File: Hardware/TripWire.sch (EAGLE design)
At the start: 40 parts, among them X1 GADGETEER-SOCKET

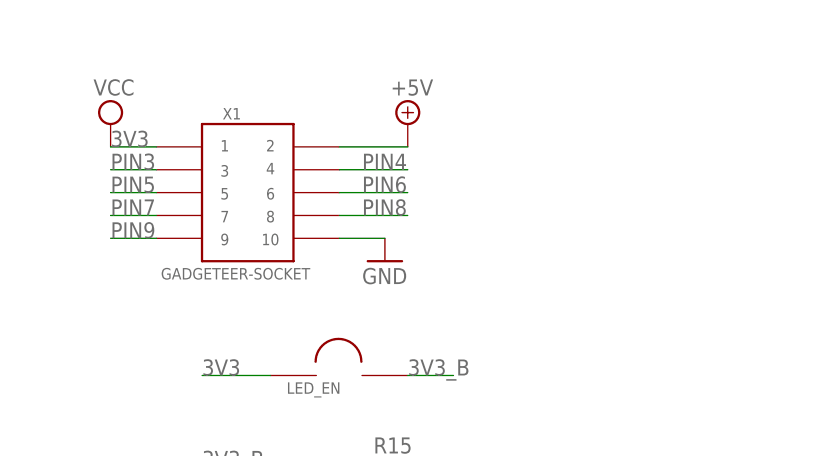
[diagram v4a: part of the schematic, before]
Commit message: Added pin breakout for non-Gadgeteer use.
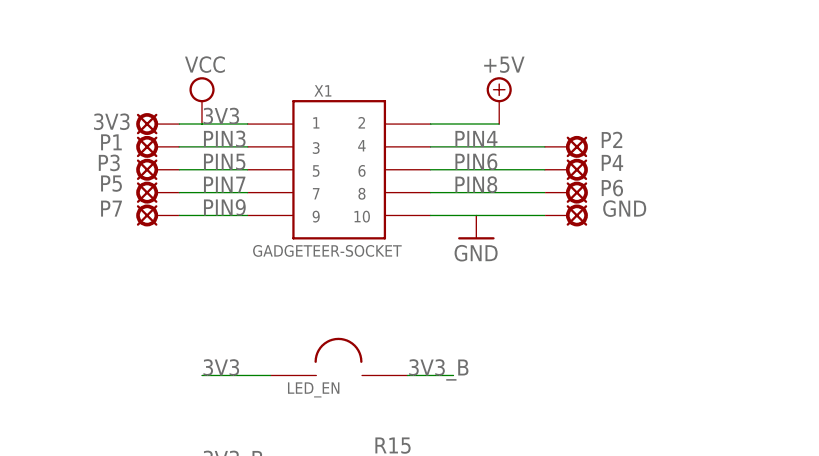
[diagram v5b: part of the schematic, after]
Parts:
- added 3V3, GND, P1, P2, P3, P4, P5, P6, P7: LSP11, solpad:LSP11
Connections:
- net 3V3: now also 3V3.MP
- net GND: now also GND.MP
- net PIN3: now also P1.MP
- net PIN4: now also P2.MP
- net PIN5: now also P3.MP
- net PIN6: now also P4.MP
- net PIN7: now also P5.MP
- net PIN8: now also P6.MP
- net PIN9: now also P7.MP
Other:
- moved on the sheet: X1
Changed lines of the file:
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@@
 <part name="R21" library="SparkFun-Resistors" deviceset="RESISTOR" device="0603-RES" value="33"/>
 <part name="LED_EN" library="SoftDust" deviceset="SOLDER-JUNCTION" device=""/>
+<part name="P2" library="solpad" deviceset="LSP11" device=""/>
+<part name="P4" library="solpad" deviceset="LSP11" device=""/>
+<part name="P6" library="solpad" deviceset="LSP11" device=""/>
+<part name="GND" library="solpad" deviceset="LSP11" device=""/>
+<part name="3V3" library="solpad" deviceset="LSP11" device=""/>
+<part name="P1" library="solpad" deviceset="LSP11" device=""/>
+<part name="P3" library="solpad" deviceset="LSP11" device=""/>
+<part name="P5" library="solpad" deviceset="LSP11" device=""/>
+<part name="P7" library="solpad" deviceset="LSP11" device=""/>
 </parts>
 <sheets>
@@
 <instances>
 <instance part="FRAME2" gate="G$1" x="0" y="0"/>
-<instance part="GND1" gate="1" x="45.72" y="101.6"/>
-<instance part="V1" gate="+5V" x="48.26" y="116.84"/>
-<instance part="V2" gate="G$1" x="15.24" y="116.84"/>
-<instance part="X1" gate="G$1" x="30.48" y="109.22" smashed="yes">
-<attribute name="NAME" x="27.686" y="117.348" size="1.27" layer="95"/>
-<attribute name="VALUE" x="20.828" y="99.568" size="1.27" layer="96"/>
+<instance part="GND1" gate="1" x="55.88" y="104.14"/>
+<instance part="V1" gate="+5V" x="58.42" y="119.38"/>
+<instance part="V2" gate="G$1" x="25.4" y="119.38"/>
+<instance part="X1" gate="G$1" x="40.64" y="111.76" smashed="yes">
+<attribute name="NAME" x="37.846" y="119.888" size="1.27" layer="95"/>
+<attribute name="VALUE" x="30.988" y="102.108" size="1.27" layer="96"/>
 </instance>
 <instance part="LOGO1" gate="G$1" x="10.16" y="7.62"/>
@@
 <attribute name="NAME" x="34.798" y="86.868" size="1.27" layer="95"/>
 </instance>
+<instance part="P2" gate="1" x="66.04" y="114.3" smashed="yes" rot="R270">
+<attribute name="NAME" x="69.596" y="114.173" size="1.778" layer="95"/>
+</instance>
+<instance part="P4" gate="1" x="66.04" y="111.76" smashed="yes" rot="R270">
+<attribute name="NAME" x="69.596" y="111.633" size="1.778" layer="95"/>
+</instance>
+<instance part="P6" gate="1" x="66.04" y="109.22" smashed="yes" rot="R270">
+<attribute name="NAME" x="69.596" y="108.839" size="1.778" layer="95"/>
+</instance>
+<instance part="GND" gate="1" x="66.04" y="106.68" smashed="yes" rot="R270">
+<attribute name="NAME" x="69.85" y="106.553" size="1.778" layer="95"/>
+</instance>
+<instance part="3V3" gate="1" x="20.32" y="116.84" smashed="yes" rot="R90">
+<attribute name="NAME" x="17.526" y="117.983" size="1.778" layer="95" rot="R180"/>
+</instance>
+<instance part="P1" gate="1" x="20.32" y="114.3" smashed="yes" rot="R90">
+<attribute name="NAME" x="13.97" y="113.919" size="1.778" layer="95"/>
+</instance>
+<instance part="P3" gate="1" x="20.32" y="111.76" smashed="yes" rot="R90">
+<attribute name="NAME" x="13.716" y="111.633" size="1.778" layer="95"/>
+</instance>
+<instance part="P5" gate="1" x="20.32" y="109.22" smashed="yes" rot="R90">
+<attribute name="NAME" x="13.97" y="109.347" size="1.778" layer="95"/>
+</instance>
+<instance part="P7" gate="1" x="20.32" y="106.68" smashed="yes" rot="R90">
+<attribute name="NAME" x="13.97" y="106.553" size="1.778" layer="95"/>
+</instance>
 </instances>
 <busses>
@@
 <net name="3V3" class="1">
 <segment>
-<wire x1="15.24" y1="114.3" x2="20.32" y2="114.3" width="0.1524" layer="91"/>
 <pinref part="V2" gate="G$1" pin="VCC"/>
 <pinref part="X1" gate="G$1" pin="P$1"/>
-<label x="15.24" y="114.3" size="1.778" layer="95"/>
+<label x="25.4" y="116.84" size="1.778" layer="95"/>
+<pinref part="3V3" gate="1" pin="MP"/>
+<wire x1="25.4" y1="116.84" x2="30.48" y2="116.84" width="0.1524" layer="91"/>
+<wire x1="22.86" y1="116.84" x2="25.4" y2="116.84" width="0.1524" layer="91"/>
 </segment>
 <segment>
@@
 <net name="GND" class="1">
 <segment>
-<wire x1="45.72" y1="104.14" x2="40.64" y2="104.14" width="0.1524" layer="91"/>
+<wire x1="55.88" y1="106.68" x2="50.8" y2="106.68" width="0.1524" layer="91"/>
 <pinref part="GND1" gate="1" pin="GND"/>
 <pinref part="X1" gate="G$1" pin="P$10"/>
+<pinref part="GND" gate="1" pin="MP"/>
+<wire x1="63.5" y1="106.68" x2="55.88" y2="106.68" width="0.1524" layer="91"/>
 </segment>
 <segment>
@@
 <net name="+5V" class="1">
 <segment>
-<wire x1="48.26" y1="114.3" x2="40.64" y2="114.3" width="0.1524" layer="91"/>
+<wire x1="58.42" y1="116.84" x2="50.8" y2="116.84" width="0.1524" layer="91"/>
 <pinref part="V1" gate="+5V" pin="+5V"/>
 <pinref part="X1" gate="G$1" pin="P$2"/>
@@
 <segment>
 <pinref part="X1" gate="G$1" pin="P$3"/>
-<wire x1="20.32" y1="111.76" x2="15.24" y2="111.76" width="0.1524" layer="91"/>
-<label x="15.24" y="111.76" size="1.778" layer="95"/>
+<wire x1="30.48" y1="114.3" x2="22.86" y2="114.3" width="0.1524" layer="91"/>
+<label x="25.4" y="114.3" size="1.778" layer="95"/>
+<pinref part="P1" gate="1" pin="MP"/>
 </segment>
 <segment>
@@
 <segment>
 <pinref part="X1" gate="G$1" pin="P$4"/>
-<wire x1="40.64" y1="111.76" x2="48.26" y2="111.76" width="0.1524" layer="91"/>
-<label x="43.18" y="111.76" size="1.778" layer="95"/>
+<wire x1="50.8" y1="114.3" x2="63.5" y2="114.3" width="0.1524" layer="91"/>
+<label x="53.34" y="114.3" size="1.778" layer="95"/>
+<pinref part="P2" gate="1" pin="MP"/>
 </segment>
 <segment>
@@
 <segment>
 <pinref part="X1" gate="G$1" pin="P$5"/>
-<wire x1="20.32" y1="109.22" x2="15.24" y2="109.22" width="0.1524" layer="91"/>
-<label x="15.24" y="109.22" size="1.778" layer="95"/>
+<label x="25.4" y="111.76" size="1.778" layer="95"/>
+<pinref part="P3" gate="1" pin="MP"/>
+<wire x1="22.86" y1="111.76" x2="30.48" y2="111.76" width="0.1524" layer="91"/>
 </segment>
 <segment>
@@
 <segment>
 <pinref part="X1" gate="G$1" pin="P$7"/>
-<wire x1="20.32" y1="106.68" x2="15.24" y2="106.68" width="0.1524" layer="91"/>
-<label x="15.24" y="106.68" size="1.778" layer="95"/>
+<label x="25.4" y="109.22" size="1.778" layer="95"/>
+<pinref part="P5" gate="1" pin="MP"/>
+<wire x1="22.86" y1="109.22" x2="30.48" y2="109.22" width="0.1524" layer="91"/>
 </segment>
 <segment>
@@
 <segment>
 <pinref part="X1" gate="G$1" pin="P$9"/>
-<wire x1="20.32" y1="104.14" x2="15.24" y2="104.14" width="0.1524" layer="91"/>
-<label x="15.24" y="104.14" size="1.778" layer="95"/>
+<label x="25.4" y="106.68" size="1.778" layer="95"/>
+<pinref part="P7" gate="1" pin="MP"/>
+<wire x1="22.86" y1="106.68" x2="30.48" y2="106.68" width="0.1524" layer="91"/>
 </segment>
 <segment>
@@
 <segment>
 <pinref part="X1" gate="G$1" pin="P$6"/>
-<wire x1="40.64" y1="109.22" x2="48.26" y2="109.22" width="0.1524" layer="91"/>
-<label x="43.18" y="109.22" size="1.778" layer="95"/>
+<wire x1="50.8" y1="111.76" x2="63.5" y2="111.76" width="0.1524" layer="91"/>
+<label x="53.34" y="111.76" size="1.778" layer="95"/>
+<pinref part="P4" gate="1" pin="MP"/>
 </segment>
 <segment>
@@
 <segment>
 <pinref part="X1" gate="G$1" pin="P$8"/>
-<wire x1="40.64" y1="106.68" x2="48.26" y2="106.68" width="0.1524" layer="91"/>
-<label x="43.18" y="106.68" size="1.778" layer="95"/>
-</segment>
-<segment>
+<wire x1="50.8" y1="109.22" x2="63.5" y2="109.22" width="0.1524" layer="91"/>
+<label x="53.34" y="109.22" size="1.778" layer="95"/>
+<pinref part="P6" gate="1" pin="MP"/>
+</segment>
+<segment>

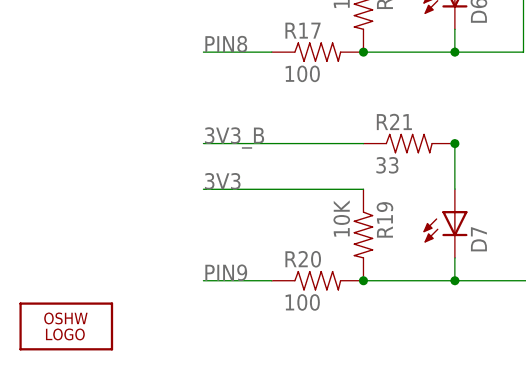
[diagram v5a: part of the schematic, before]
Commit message: Updated OSHW logo.
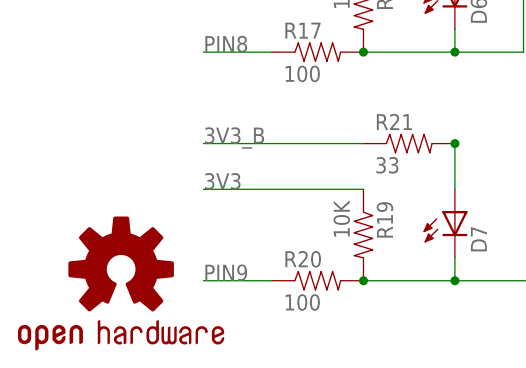
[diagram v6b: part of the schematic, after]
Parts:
- LOGO1: value LOGO-OSHW-FILLX0200-NT -> OSHW-LOGOM; device Logo:LOGO-OSHW-FILLX0200-NT -> SparkFun-Aesthetics:OSHW-LOGOM
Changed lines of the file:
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@@
 <part name="V2" library="supply2" deviceset="VCC" device=""/>
 <part name="X1" library="SoftDust" deviceset="GADGETEER-SOCKET" device=""/>
-<part name="LOGO1" library="Logo" deviceset="LOGO-OSHW-FILL" device="X0200-NT"/>
+<part name="LOGO1" library="SparkFun-Aesthetics" deviceset="OSHW-LOGO" device="M"/>
 <part name="U$1" library="SoftDust" deviceset="SPADE-TERMINAL" device="PTH"/>
 <part name="U$2" library="SoftDust" deviceset="SPADE-TERMINAL" device="PTH"/>
@@
 <attribute name="VALUE" x="30.988" y="102.108" size="1.27" layer="96"/>
 </instance>
-<instance part="LOGO1" gate="G$1" x="10.16" y="7.62"/>
+<instance part="LOGO1" gate="G$1" x="16.256" y="13.97"/>
 <instance part="U$1" gate="G$1" x="119.38" y="109.22"/>
 <instance part="U$2" gate="G$1" x="119.38" y="106.68"/>

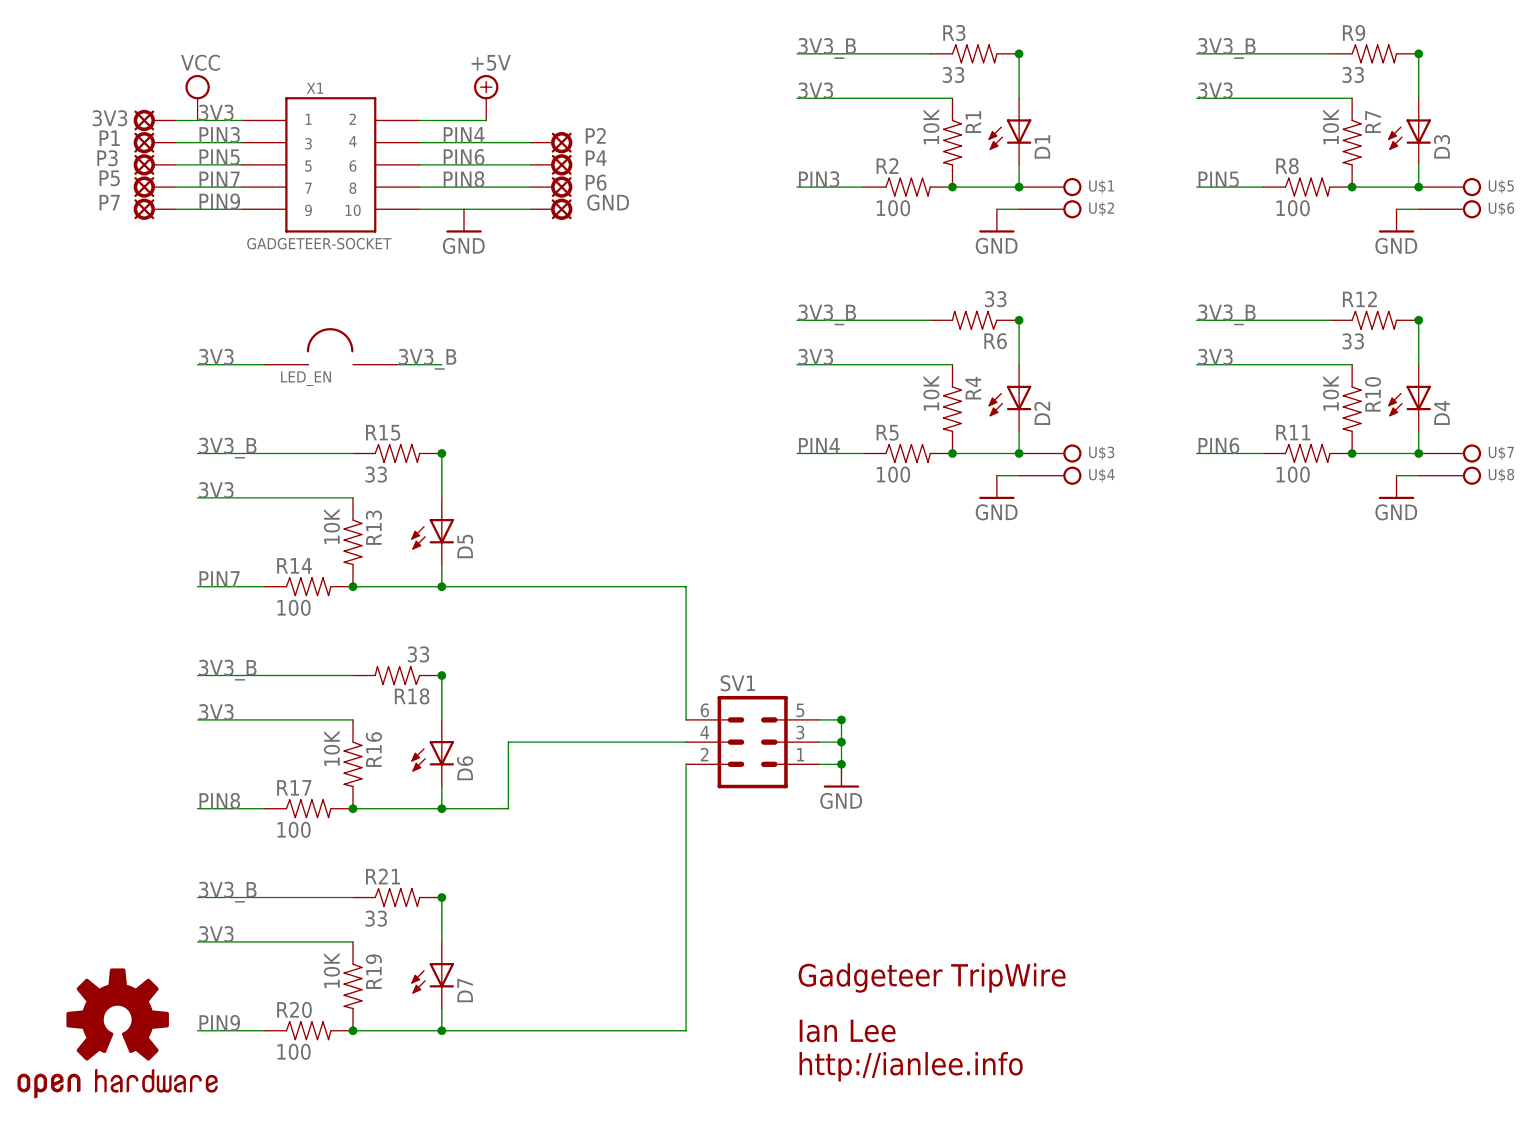
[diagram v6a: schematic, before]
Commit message: Added pin protection diodes.
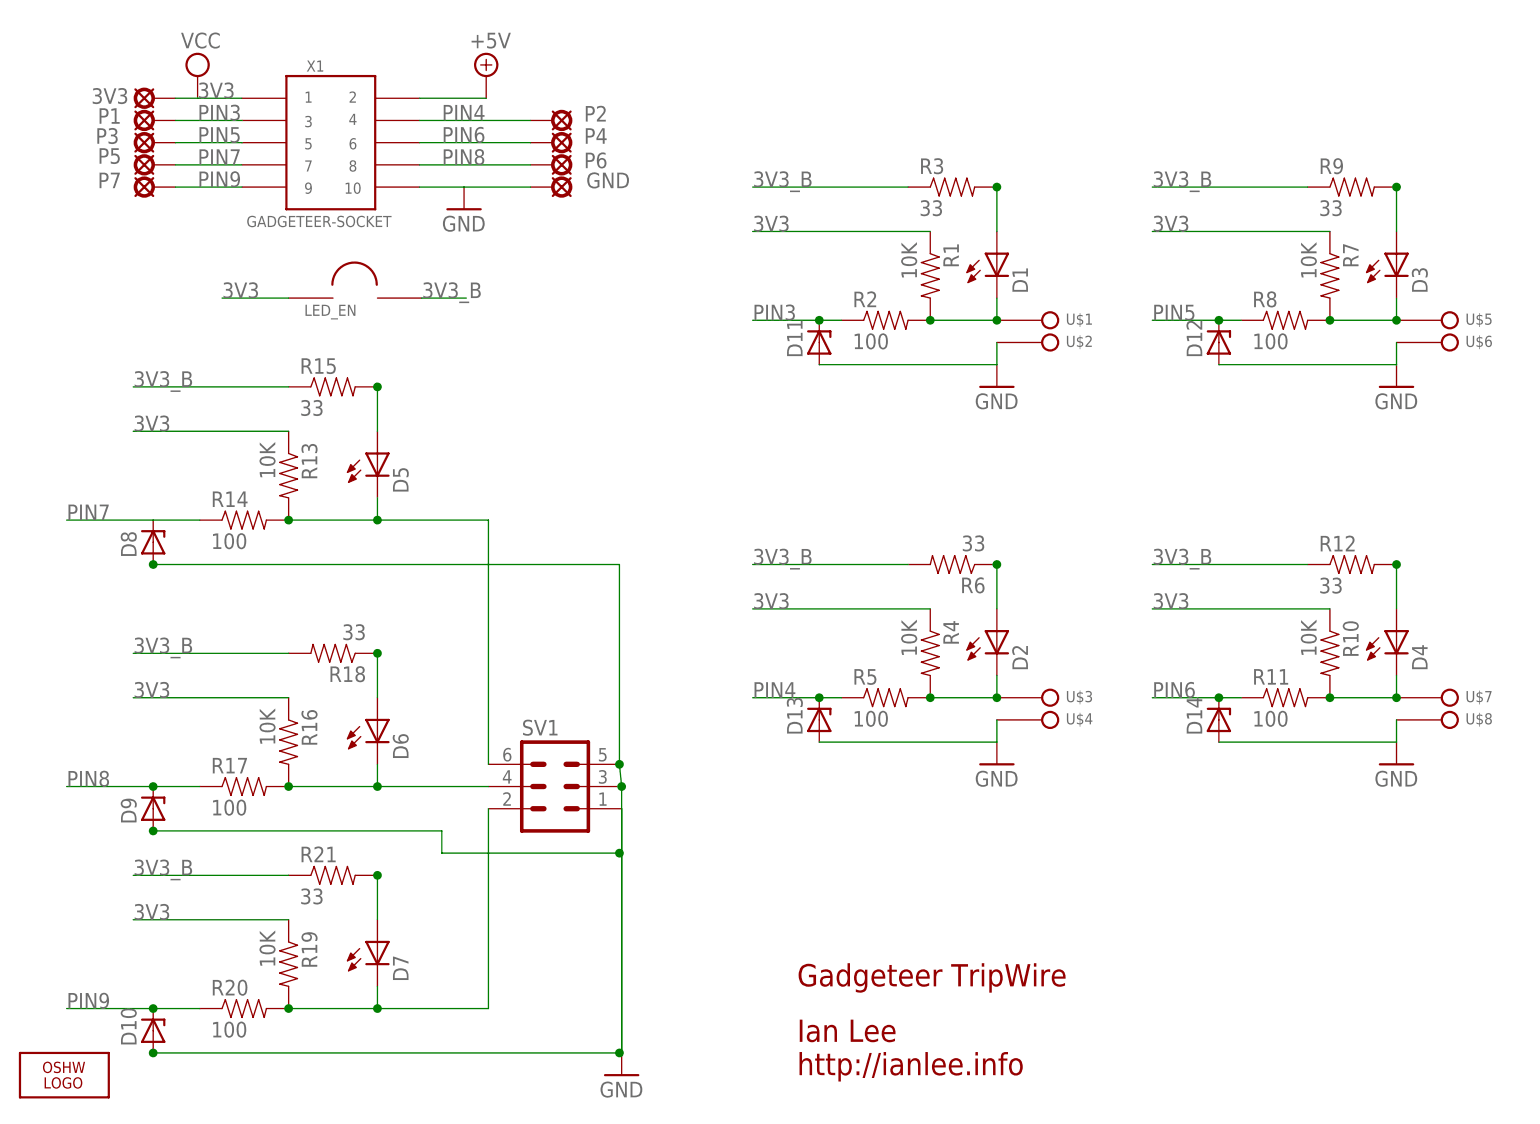
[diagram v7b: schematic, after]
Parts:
- added D10, D11, D12, D13, D14, D8, D9: (no value), diode:ZENER-DIODESOD80C
- LOGO1: value OSHW-LOGOM -> LOGO-OSHW-FILLX0200-NT; device SparkFun-Aesthetics:OSHW-LOGOM -> Logo:LOGO-OSHW-FILLX0200-NT
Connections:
- new net N$15: D9.A
- new net N$16: D10.A
- net GND: now also D11.A, D12.A, D13.A, D14.A, D8.A
- net PIN3: now also D11.C
- net PIN4: now also D13.C
- net PIN5: now also D12.C
- net PIN6: now also D14.C
- net PIN7: now also D8.C
- net PIN8: now also D9.C
- net PIN9: now also D10.C
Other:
- moved on the sheet: 3V3, D1, D2, D3, D4, D5, D6, D7, GND, LED_EN, P1, P2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
